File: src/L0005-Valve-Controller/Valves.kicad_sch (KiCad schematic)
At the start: 60 parts, among them K1 AQH0223AX, K2 AQH0223AX, K3 AQH0223AX, K4 AQH0223AX, K5 AQH0223AX, K6 AQH0223AX, P10 353620650, P11 353620650, P12 353620650, P13 353620650, P3 647676-3, P4 647676-3, P5 647676-3, P6 647676-3, P7 647676-3, P8 647676-3, Q1 CMLDM7003, Q2 CMLDM7003, U3 MAX3370EXK+T, U4 MAX3370EXK+T

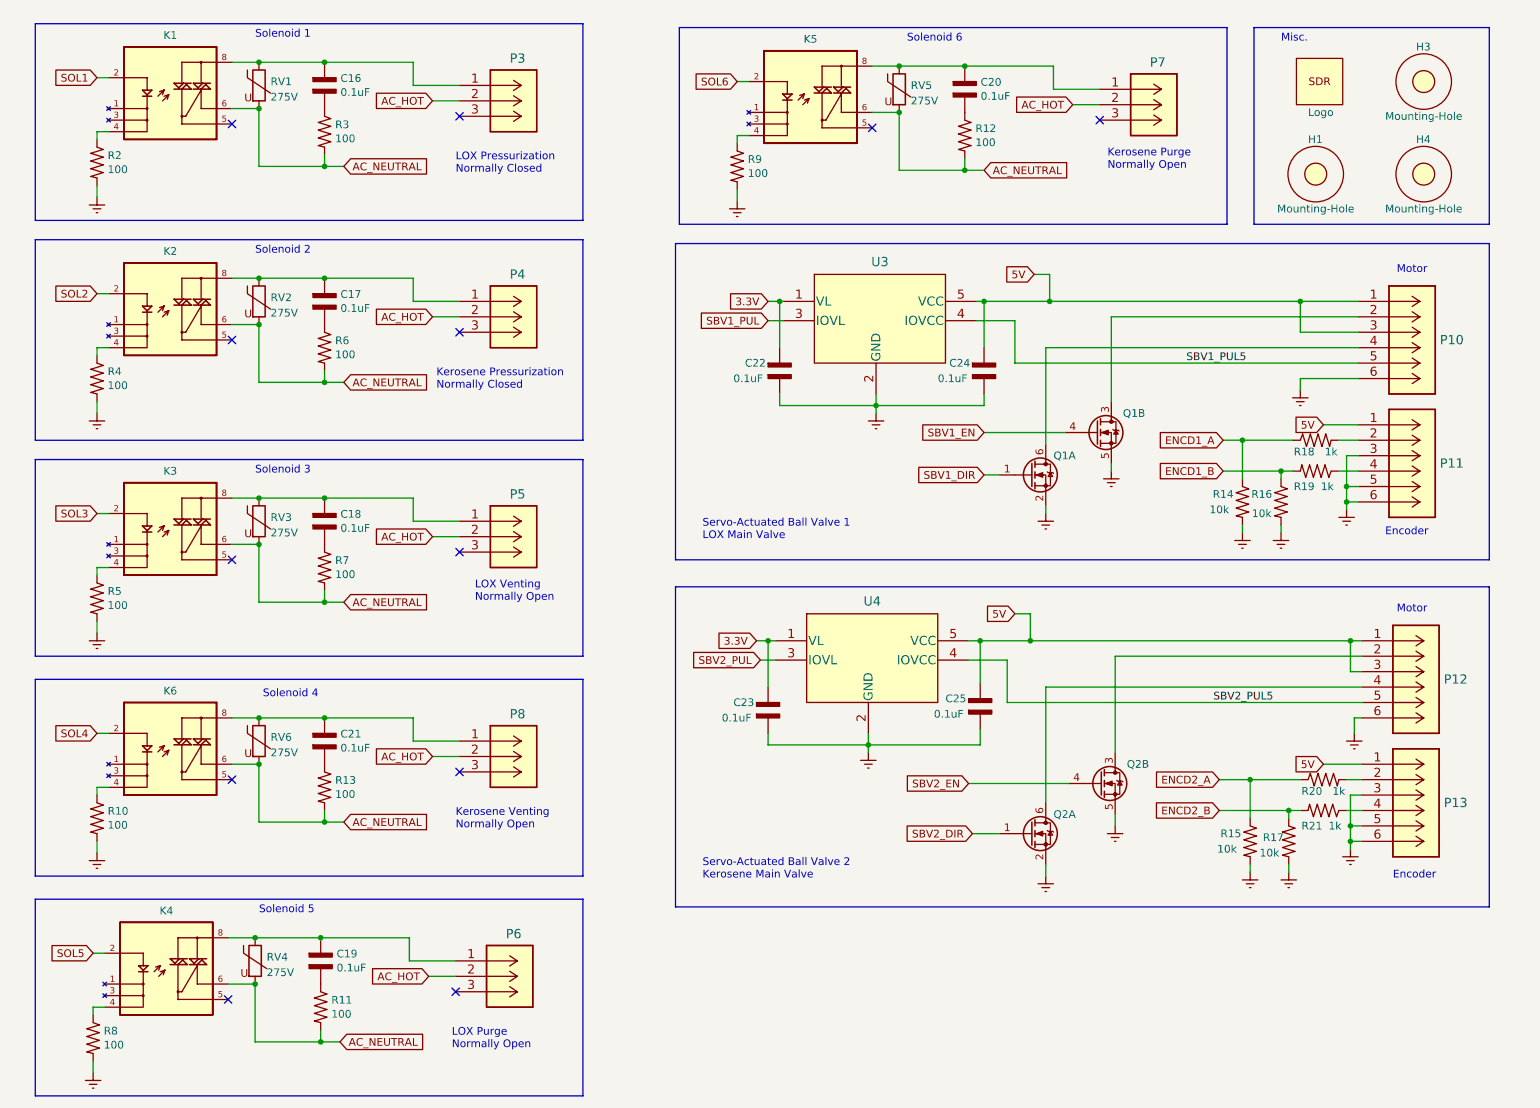
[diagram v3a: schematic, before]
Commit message: added solenoid control decoder
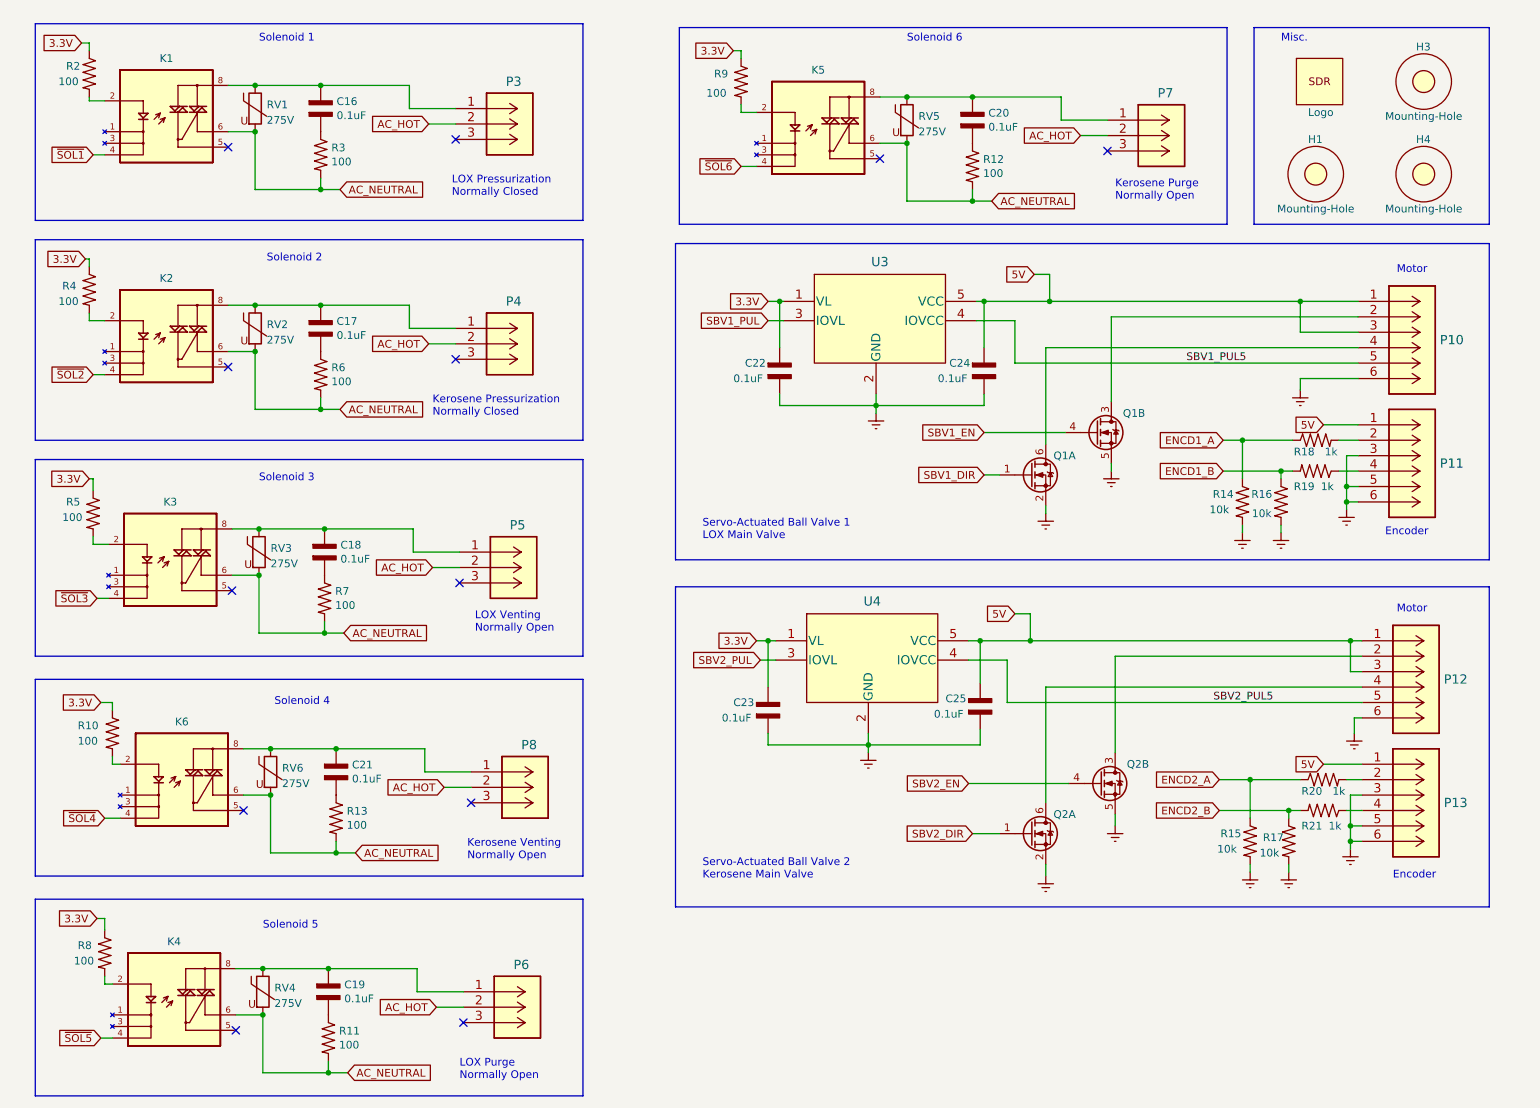
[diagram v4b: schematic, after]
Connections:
- net 3.3V: now also R10.1, R2.1, R4.1, R5.1, R8.1, R9.1
- net Earth: no longer R10.2, R2.2, R4.2, R5.2, R8.2, R9.2
- net ~{SOL1}: now reaches K1.4
- net ~{SOL1}: no longer R2.1
- net ~{SOL2}: now reaches K2.4
- net ~{SOL2}: no longer R4.1
- net ~{SOL3}: now reaches K3.4
- net ~{SOL3}: no longer R5.1
- net ~{SOL4}: now reaches K6.4
- net ~{SOL4}: no longer R10.1
- net ~{SOL5}: now reaches K4.4
- net ~{SOL5}: no longer R8.1
- net ~{SOL6}: now reaches K5.4
- net ~{SOL6}: no longer R9.1
- net SOL1: no longer names the net of K1.2
- net SOL1: now also R2.2
- net SOL2: no longer names the net of K2.2
- net SOL2: now also R4.2
- net SOL3: no longer names the net of K3.2
- net SOL3: now also R5.2
- net SOL4: no longer names the net of K6.2
- net SOL4: now also R10.2
- net SOL5: no longer names the net of K4.2
- net SOL5: now also R8.2
- net SOL6: no longer names the net of K5.2
- net SOL6: now also R9.2
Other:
- moved on the sheet: C16, C17, C18, C19, C20, C21, K1, K2, K3, K4, K5, K6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

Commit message: added STM32H7 MCU
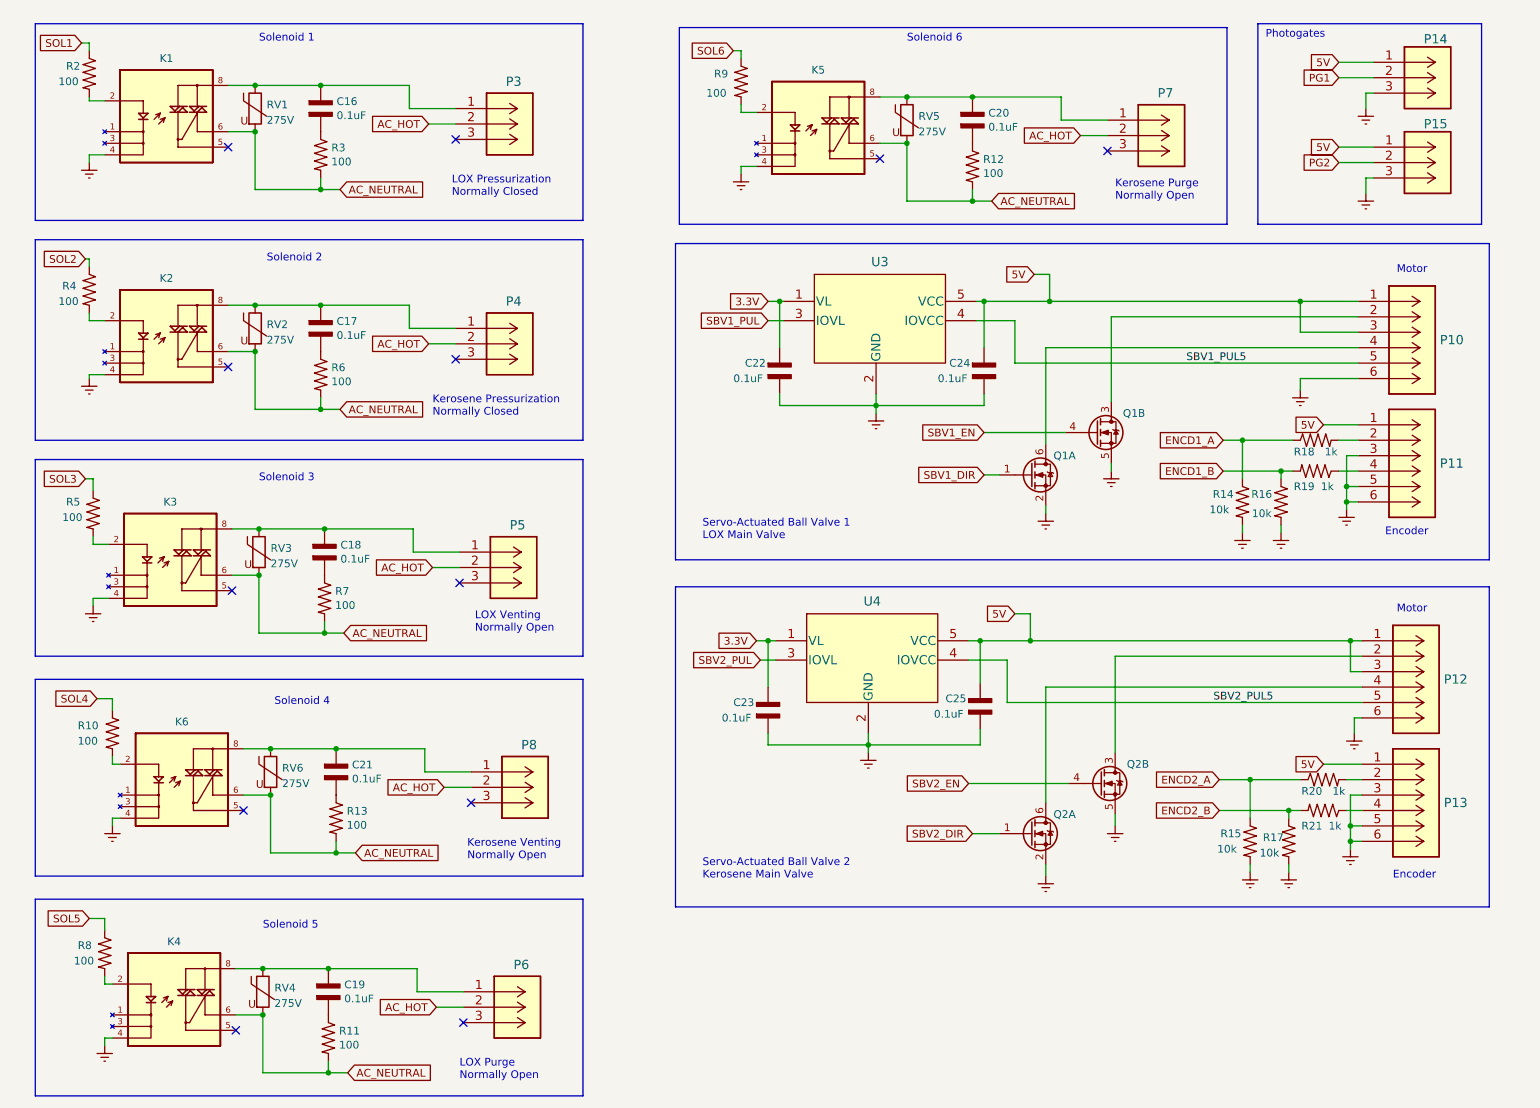
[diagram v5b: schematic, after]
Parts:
- removed H1, H3, H4: Mounting-Hole, L0005-Valve-Controller:MountingHole_4.3mm_M4_DIN965, symbol L0005-Valve-Controller:Mounting-Hole
- removed LOGO1: Logo, L0005-Valve-Controller:Logo, symbol L0005-Valve-Controller:Logo
- added P14, P15: 647676-3, L0005-Valve-Controller:647676-3, symbol L0005-Valve-Controller:647676-3
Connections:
- net ~{SOL1} is gone; now on net Earth: K1.4
- net ~{SOL2} is gone; now on net Earth: K2.4
- net ~{SOL3} is gone; now on net Earth: K3.4
- net ~{SOL4} is gone; now on net Earth: K6.4
- net ~{SOL5} is gone; now on net Earth: K4.4
- net ~{SOL6} is gone; now on net Earth: K5.4
- net 3.3V: no longer R10.1, R2.1, R4.1, R5.1, R8.1, R9.1
- net 5V: now also P14.1, P15.1
- net Earth: now also P14.3, P15.3
- new net PG1: P14.2
- new net PG2: P15.2
- new net SOL1: R2.1
- new net SOL2: R4.1
- new net SOL3: R5.1
- new net SOL4: R10.1
- new net SOL5: R8.1
- new net SOL6: R9.1
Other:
- note added: "Photogates"
- note removed: "Misc."

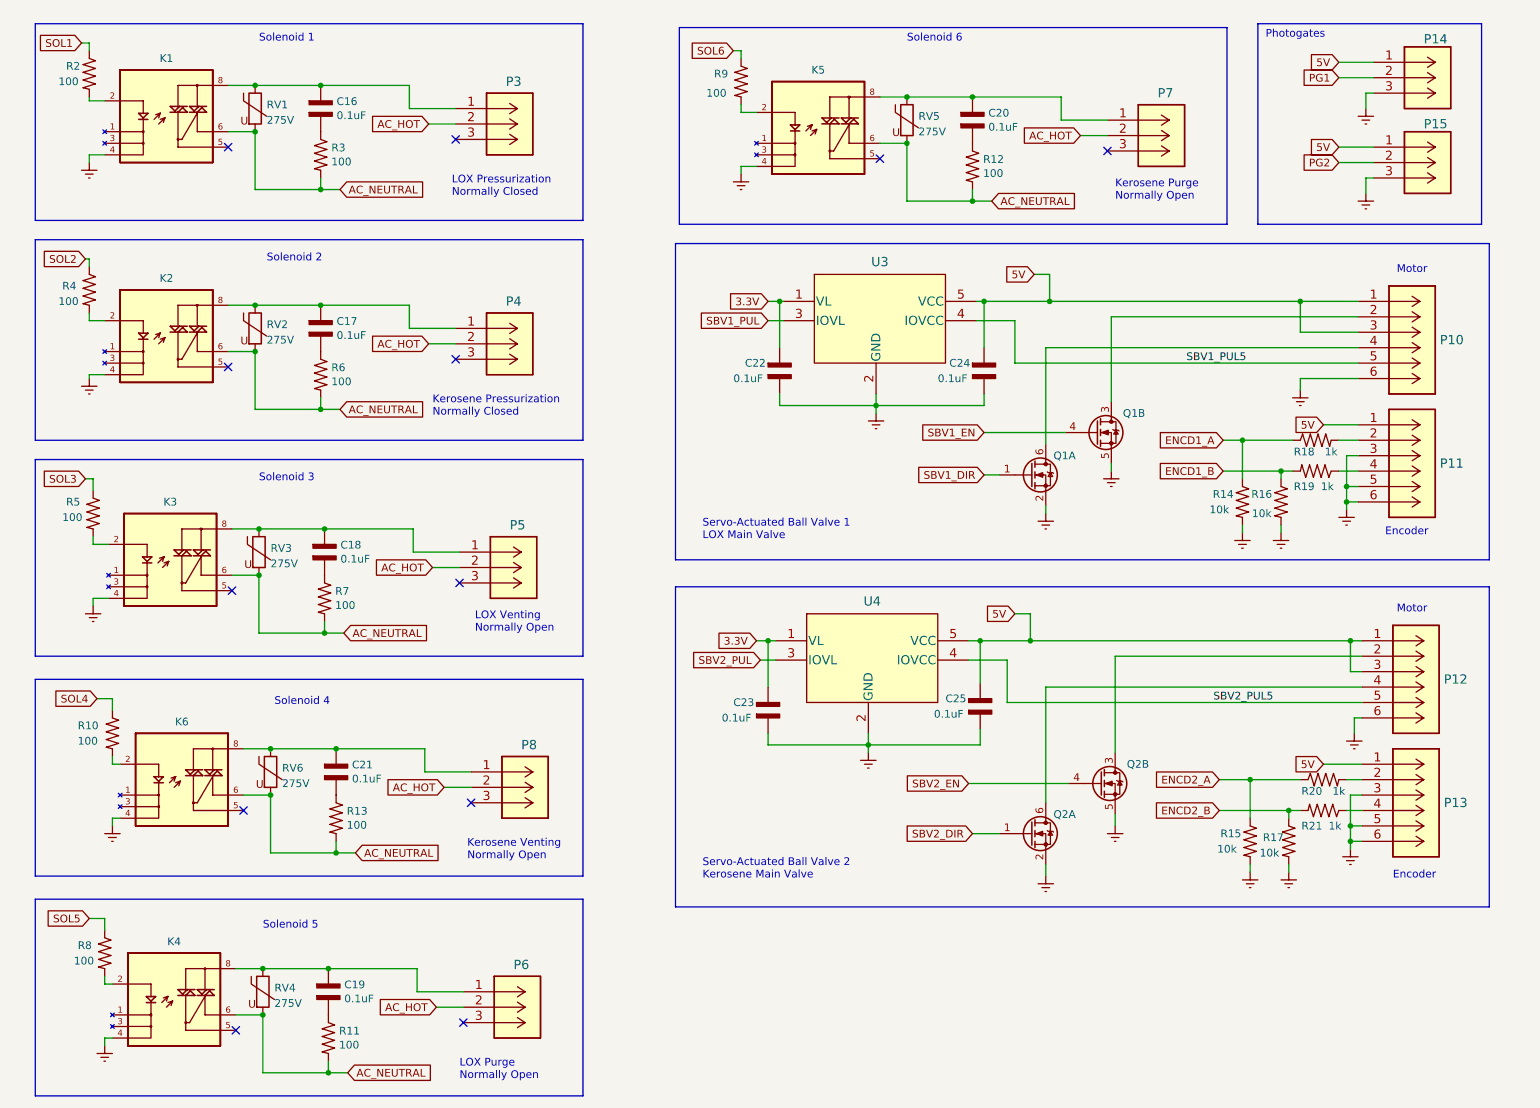
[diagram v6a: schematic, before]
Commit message: changed level shifter to opendrain mosfet for pulse interface
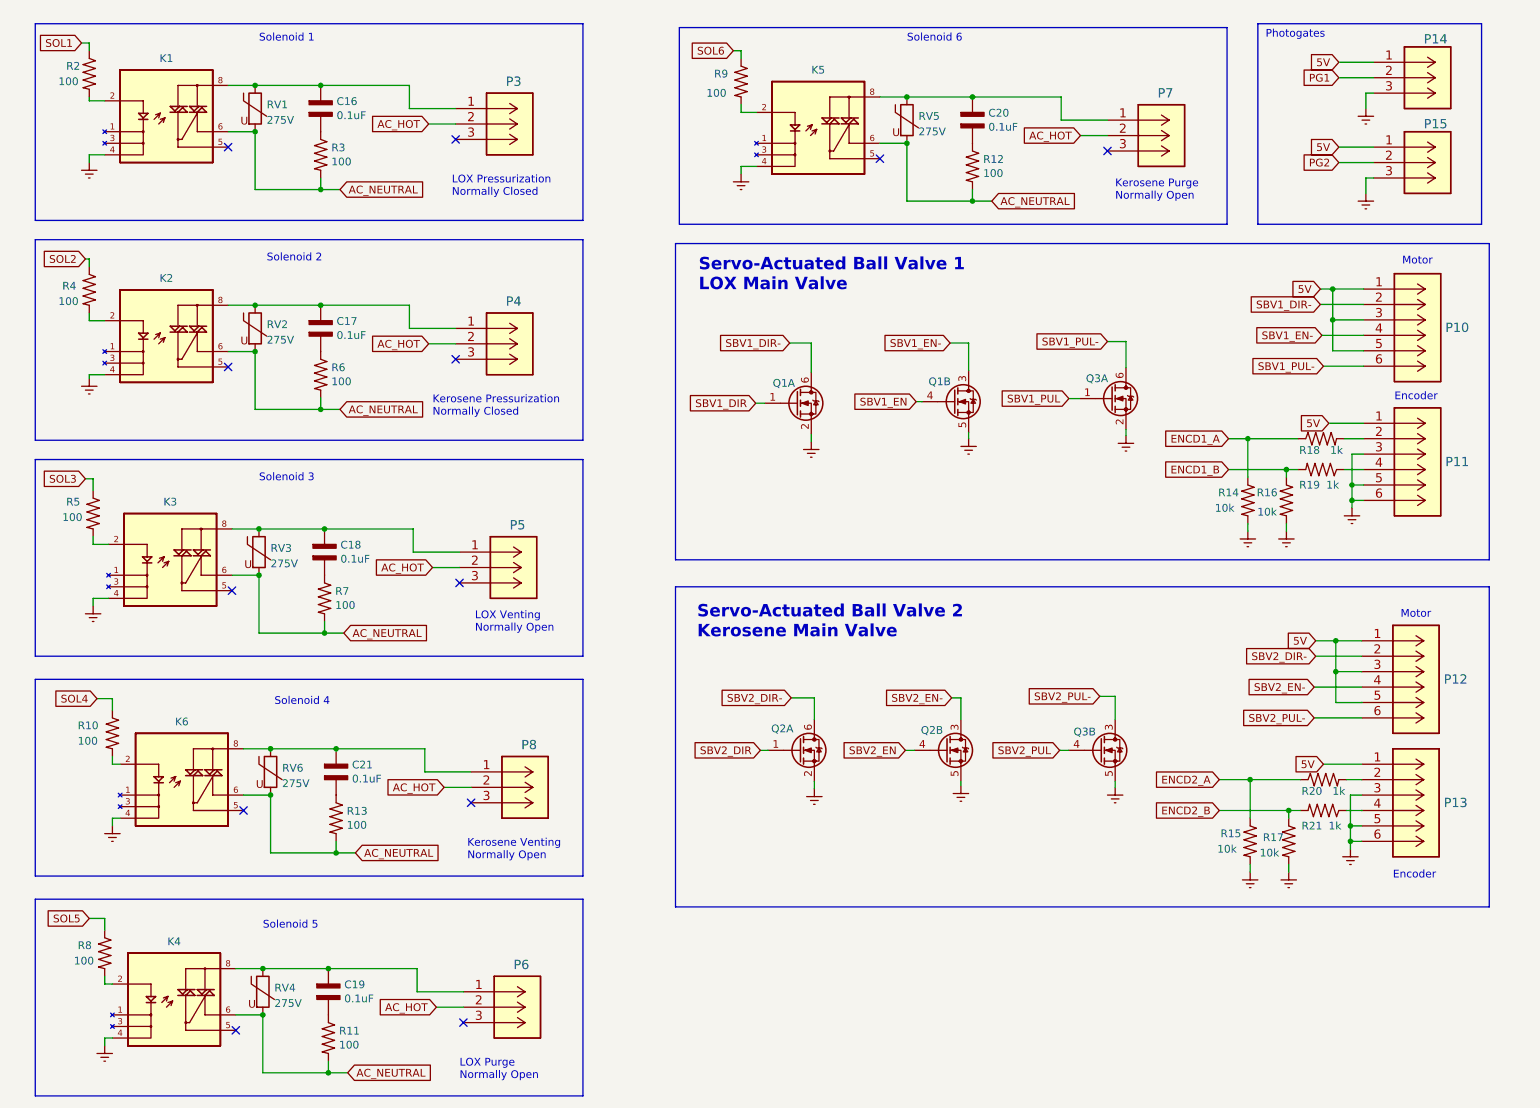
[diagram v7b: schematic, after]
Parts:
- removed C22, C23, C24, C25: 0.1uF, L0005-Valve-Controller:CAP_0603, symbol L0005-Valve-Controller:CAP_0603
- removed U3, U4: MAX3370EXK+T, L0005-Valve-Controller:MAX3370EXK&plus_T, symbol L0005-Valve-Controller:MAX3370EXK+T
- added Q3: CMLDM7003, Package_TO_SOT_THT:TO-92_Inline, symbol L0005-Valve-Controller:CMLDM7003
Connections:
- net SBV1_PUL5 is gone; now on net 5V: P10.5
- net SBV2_PUL5 is gone; now on net 5V: P12.5
- net Earth: now also Q3.2 (S), Q3.5 (S); no longer P10.6, P12.6
- net SBV1_PUL: now also Q3.1 (G)
- net SBV2_PUL: now also Q3.4 (G)
- net SBV2_DIR-: now reaches Q2.6 (D)
- net SBV2_DIR-: now also P12.2 (GND); no longer P12.4
- net SBV2_EN-: now reaches Q2.3 (D)
- net SBV2_EN-: now also P12.4; no longer P12.2 (GND)
- net SBV1_DIR-: now reaches Q1.6 (D)
- net SBV1_DIR-: now also P10.2 (GND); no longer P10.4
- net SBV1_EN-: now reaches Q1.3 (D)
- net SBV1_EN-: now also P10.4; no longer P10.2 (GND)
- new net SBV1_PUL-: P10.6, Q3.6 (D)
- new net SBV2_PUL-: P12.6, Q3.3 (D)
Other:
- moved on the sheet: P10, P11, Q1A, Q1B, Q2A, Q2B, R14, R16, R18, R19

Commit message: finalized schematic
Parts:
- Q3: footprint Package_TO_SOT_THT:TO-92_Inline -> L0005-Valve-Controller:CMLDM7003 TR
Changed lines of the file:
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@@
       (effects (font (size 1.27 1.27)) (justify left) hide)
     )
-    (property "Footprint" "Package_TO_SOT_THT:TO-92_Inline" (at 201.676 142.748 0)
+    (property "Footprint" "L0005-Valve-Controller:CMLDM7003 TR" (at 201.676 142.748 0)
       (effects (font (size 1.27 1.27) italic) (justify left) hide)
     )
